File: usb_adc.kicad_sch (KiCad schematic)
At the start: 17 parts, among them IC1 PCM2903CDBR, U3 74LVC1G08, X1 ECS-120-8-36-CKM-TR3

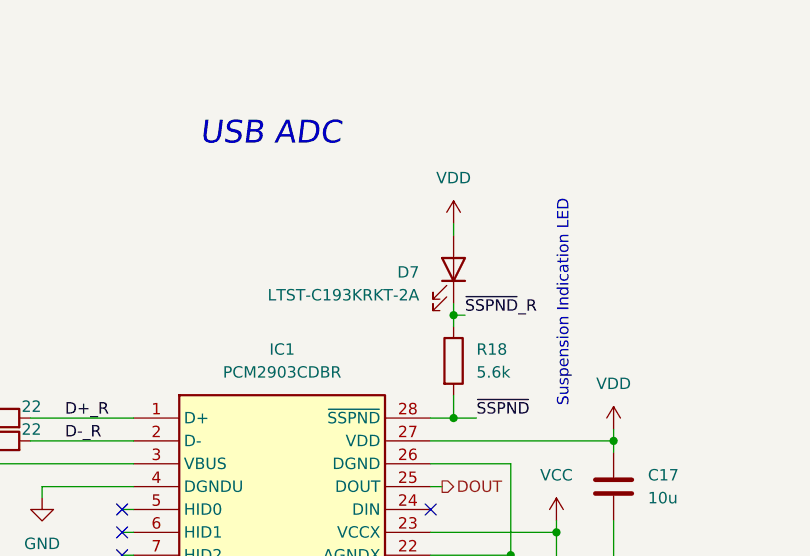
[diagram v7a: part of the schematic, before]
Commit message: Reannotated schematic + restarted layout
woohoo
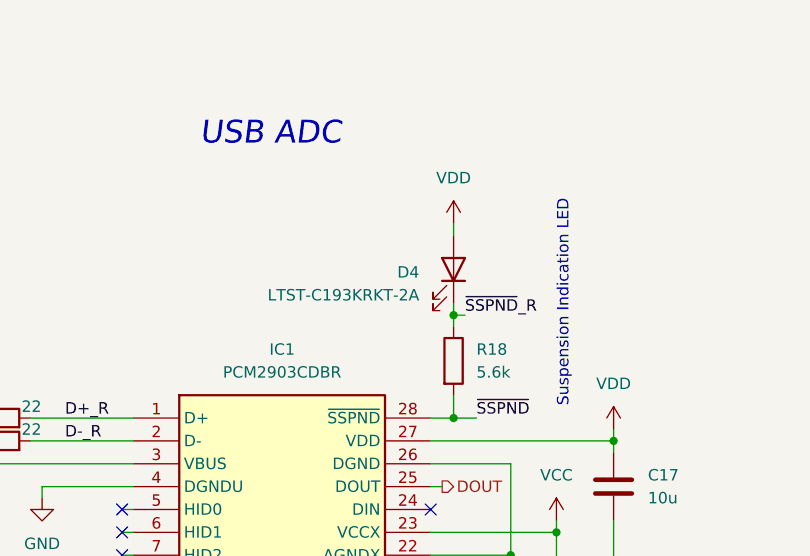
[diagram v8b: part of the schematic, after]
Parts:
- renumbered D7 to D4
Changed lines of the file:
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@@
 		(dnp no)
 		(fields_autoplaced yes)
-		(property "Reference" "#PWR023"
+		(property "Reference" "#PWR022"
 			(at 149.86 87.63 0)
 			(effects
@@
 			(project "BinauralMic"
 				(path "/d9e790b9-8aa4-4e58-8bd7-6ef4bc890627/1f1de066-50ca-4c06-9457-56cc25f04510"
-					(reference "#PWR023")
+					(reference "#PWR022")
 					(unit 1)
 				)
@@
 		(dnp no)
 		(fields_autoplaced yes)
-		(property "Reference" "#PWR024"
+		(property "Reference" "#PWR023"
 			(at 86.36 97.79 0)
 			(effects
@@
 			(project "BinauralMic"
 				(path "/d9e790b9-8aa4-4e58-8bd7-6ef4bc890627/1f1de066-50ca-4c06-9457-56cc25f04510"
-					(reference "#PWR024")
+					(reference "#PWR023")
 					(unit 1)
 				)
@@
 		(dnp no)
 		(fields_autoplaced yes)
-		(property "Reference" "#PWR025"
+		(property "Reference" "#PWR024"
 			(at 143.51 97.79 0)
 			(effects
@@
 			(project "BinauralMic"
 				(path "/d9e790b9-8aa4-4e58-8bd7-6ef4bc890627/1f1de066-50ca-4c06-9457-56cc25f04510"
-					(reference "#PWR025")
+					(reference "#PWR024")
 					(unit 1)
 				)
@@
 		(dnp no)
 		(fields_autoplaced yes)
-		(property "Reference" "#PWR026"
+		(property "Reference" "#PWR025"
 			(at 149.86 106.68 0)
 			(effects
@@
 			(project "BinauralMic"
 				(path "/d9e790b9-8aa4-4e58-8bd7-6ef4bc890627/1f1de066-50ca-4c06-9457-56cc25f04510"
-					(reference "#PWR026")
+					(reference "#PWR025")
 					(unit 1)
 				)
@@
 		(dnp no)
 		(fields_autoplaced yes)
-		(property "Reference" "#PWR028"
+		(property "Reference" "#PWR027"
 			(at 212.09 115.57 0)
 			(effects
@@
 			(project "BinauralMic"
 				(path "/d9e790b9-8aa4-4e58-8bd7-6ef4bc890627/1f1de066-50ca-4c06-9457-56cc25f04510"
-					(reference "#PWR028")
+					(reference "#PWR027")
 					(unit 1)
 				)
@@
 		(dnp no)
 		(fields_autoplaced yes)
-		(property "Reference" "#PWR021"
+		(property "Reference" "#PWR020"
 			(at 205.74 82.55 0)
 			(effects
@@
 			(project "BinauralMic"
 				(path "/d9e790b9-8aa4-4e58-8bd7-6ef4bc890627/1f1de066-50ca-4c06-9457-56cc25f04510"
-					(reference "#PWR021")
+					(reference "#PWR020")
 					(unit 1)
 				)
@@
 		(dnp no)
 		(fields_autoplaced yes)
-		(property "Reference" "D7"
+		(property "Reference" "D4"
 			(at 128.27 66.3574 90)
 			(effects
@@
 			(project "BinauralMic"
 				(path "/d9e790b9-8aa4-4e58-8bd7-6ef4bc890627/1f1de066-50ca-4c06-9457-56cc25f04510"
-					(reference "D7")
+					(reference "D4")
 					(unit 1)
 				)
@@
 		(dnp no)
 		(fields_autoplaced yes)
-		(property "Reference" "#PWR031"
+		(property "Reference" "#PWR030"
 			(at 208.28 138.43 0)
 			(effects
@@
 			(project "BinauralMic"
 				(path "/d9e790b9-8aa4-4e58-8bd7-6ef4bc890627/1f1de066-50ca-4c06-9457-56cc25f04510"
-					(reference "#PWR031")
+					(reference "#PWR030")
 					(unit 1)
 				)
@@
 		(dnp no)
 		(fields_autoplaced yes)
-		(property "Reference" "#PWR020"
+		(property "Reference" "#PWR019"
 			(at 177.8 67.31 0)
 			(effects
@@
 			(project "BinauralMic"
 				(path "/d9e790b9-8aa4-4e58-8bd7-6ef4bc890627/1f1de066-50ca-4c06-9457-56cc25f04510"
-					(reference "#PWR020")
+					(reference "#PWR019")
 					(unit 1)
 				)
@@
 		(dnp no)
 		(fields_autoplaced yes)
-		(property "Reference" "#PWR027"
+		(property "Reference" "#PWR026"
 			(at 63.5 107.95 0)
 			(effects
@@
 			(project "BinauralMic"
 				(path "/d9e790b9-8aa4-4e58-8bd7-6ef4bc890627/1f1de066-50ca-4c06-9457-56cc25f04510"
-					(reference "#PWR027")
+					(reference "#PWR026")
 					(unit 1)
 				)
@@
 		(dnp no)
 		(fields_autoplaced yes)
-		(property "Reference" "#PWR019"
+		(property "Reference" "#PWR018"
 			(at 132.08 64.77 0)
 			(effects
@@
 			(project "BinauralMic"
 				(path "/d9e790b9-8aa4-4e58-8bd7-6ef4bc890627/1f1de066-50ca-4c06-9457-56cc25f04510"
-					(reference "#PWR019")
+					(reference "#PWR018")
 					(unit 1)
 				)
@@
 		(dnp no)
 		(fields_autoplaced yes)
-		(property "Reference" "#PWR029"
+		(property "Reference" "#PWR028"
 			(at 63.5 123.19 0)
 			(effects
@@
 			(project "BinauralMic"
 				(path "/d9e790b9-8aa4-4e58-8bd7-6ef4bc890627/1f1de066-50ca-4c06-9457-56cc25f04510"
-					(reference "#PWR029")
+					(reference "#PWR028")
 					(unit 1)
 				)
@@
 		(dnp no)
 		(fields_autoplaced yes)
-		(property "Reference" "#PWR022"
+		(property "Reference" "#PWR021"
 			(at 68.58 82.55 0)
 			(effects
@@
 			(project "BinauralMic"
 				(path "/d9e790b9-8aa4-4e58-8bd7-6ef4bc890627/1f1de066-50ca-4c06-9457-56cc25f04510"
-					(reference "#PWR022")
+					(reference "#PWR021")
 					(unit 1)
 				)
@@
 		(dnp no)
 		(fields_autoplaced yes)
-		(property "Reference" "#PWR018"
+		(property "Reference" "#PWR017"
 			(at 205.74 53.34 0)
 			(effects
@@
 			(project "BinauralMic"
 				(path "/d9e790b9-8aa4-4e58-8bd7-6ef4bc890627/1f1de066-50ca-4c06-9457-56cc25f04510"
-					(reference "#PWR018")
+					(reference "#PWR017")
 					(unit 1)
 				)
@@
 		(dnp no)
 		(fields_autoplaced yes)
-		(property "Reference" "#PWR030"
+		(property "Reference" "#PWR029"
 			(at 143.51 127 0)
 			(effects
@@
 			(project "BinauralMic"
 				(path "/d9e790b9-8aa4-4e58-8bd7-6ef4bc890627/1f1de066-50ca-4c06-9457-56cc25f04510"
-					(reference "#PWR030")
-					(unit 1)
-				)
+					(reference "#PWR029")
+					(unit 1)
+				)
